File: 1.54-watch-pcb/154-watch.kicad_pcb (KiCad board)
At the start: 4 copper layers, 50 x 32.5 mm, 58 parts, among them J1 AFC24-S24FIC-00, J2 Conn_01x06_Female, J3 USB_C_Programming, J4 Jack-DC, J5 Conn_01x02_Male, Q1 Si1308, Q2 BC817, Q3 BC817, Q4 Si2301CDS, SW1 RESET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

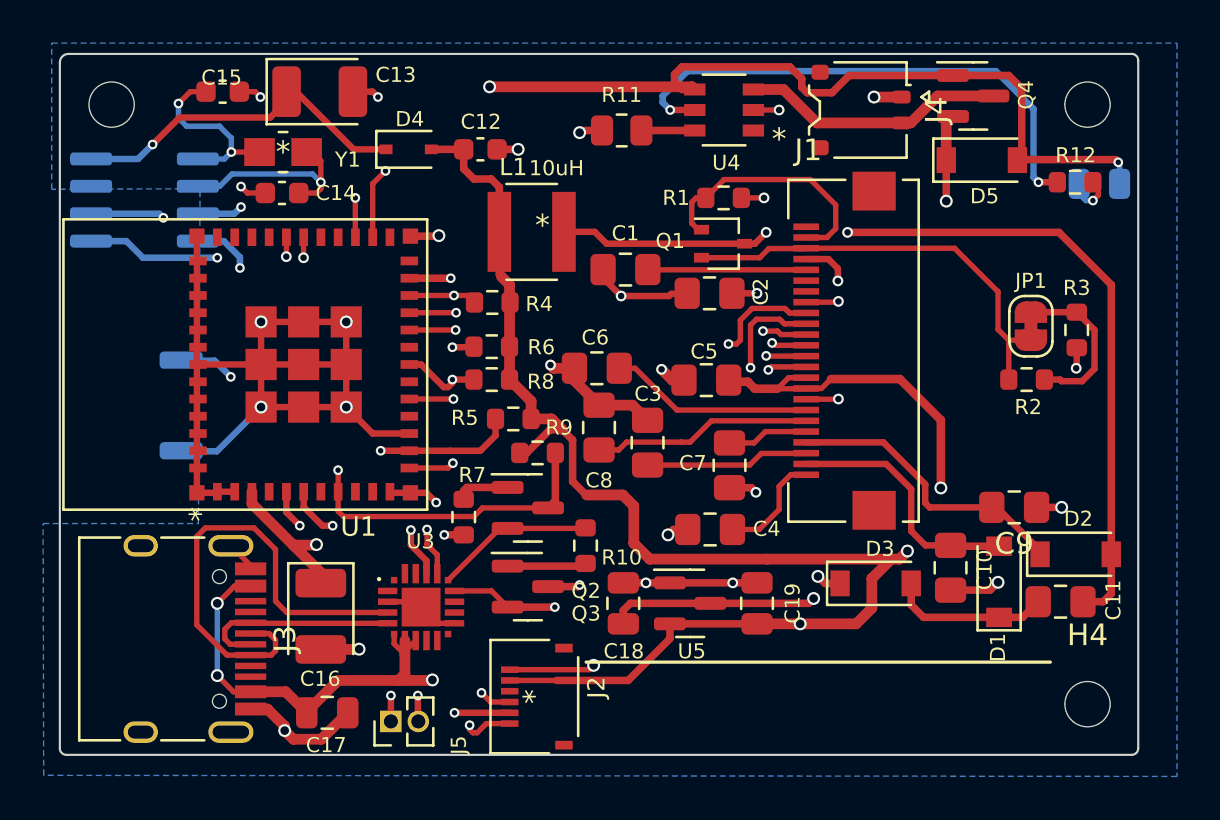
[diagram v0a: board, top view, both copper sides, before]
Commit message: #6 Make edge cut for FPC
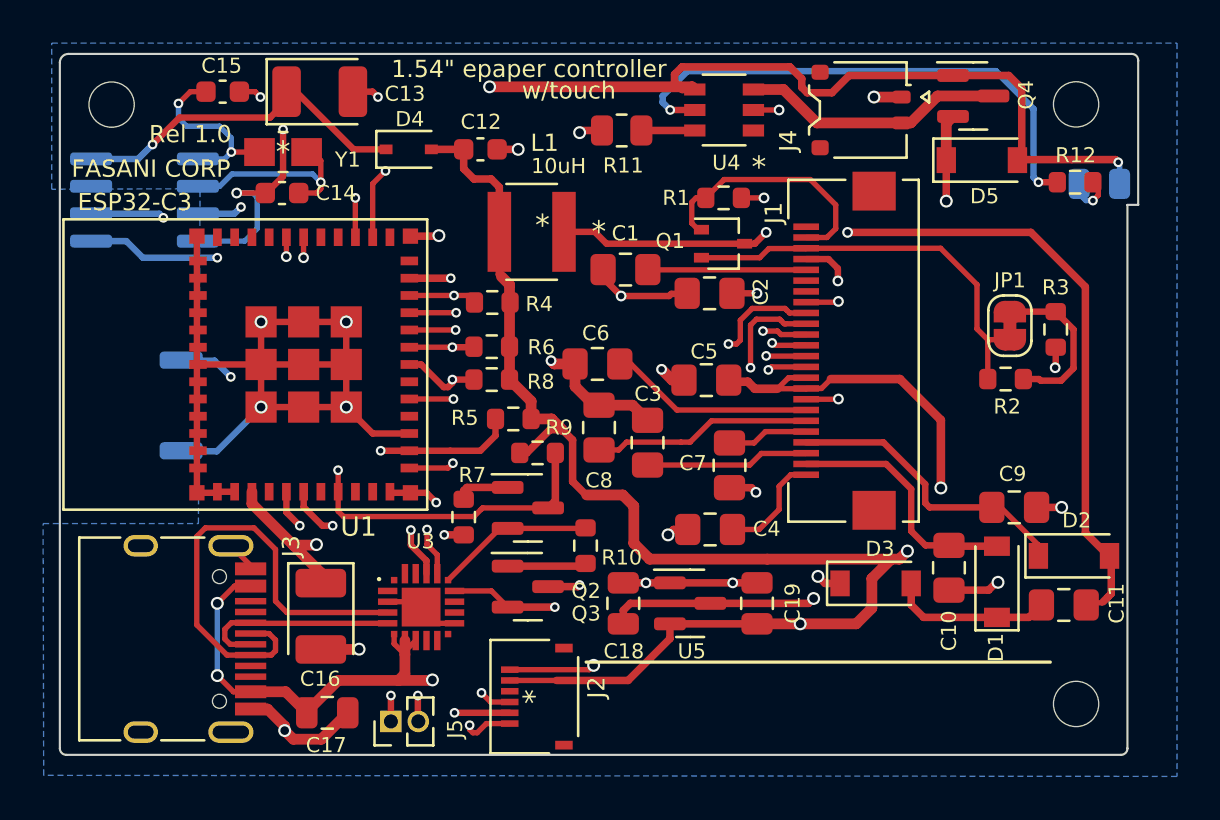
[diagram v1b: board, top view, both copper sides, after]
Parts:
- U1: value ESP32-C3-MINI-1-N4 -> ESP32-C3-MINI
- U4: value TP4057-42-SOT26-R -> SOT-23-5_TPW
- moved JP1 0.98 mm to (116.0, 42.6)
- moved R2 0.98 mm to (115.8, 45.1)
- moved R3 0.98 mm to (118.2, 42.8)
- moved H3 0.53 mm to (119.1, 32.3)
- moved H4 0.53 mm to (119.1, 60.1)
- moved C11 0.21 mm to (118.5, 55.5)
- moved C6 0.20 mm to (96.9, 44.4)
- moved D2 0.11 mm to (119.0, 53.3)
- moved D1 0.10 mm to (115.5, 54.5)
- moved C10 0.08 mm to (113.2, 53.8)
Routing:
- net GND: track 102.0 -> 108.3 mm
- net /I2C_SDA: track 43.0 -> 44.9 mm
- net Net-(J1-Pad22): track 20.1 -> 19.3 mm
- net Net-(C11-Pad2): track 42.6 -> 42.0 mm
- net PREVGH: track 13.6 -> 14.2 mm
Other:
- outline, holes or cut-outs redrawn
- board text added: "1.54{dblquote} epaper controller"
- board text added: "200x200 with optional touch panel"
- board text added: "ESP32-C3"
- board text added: "FASANI CORP"
- board text added: "GOOD-DISPLAY GDEY0154D67"
- board text added: "Rel 1.0"
- board text added: "w/touch"

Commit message: #6 Add info to silk
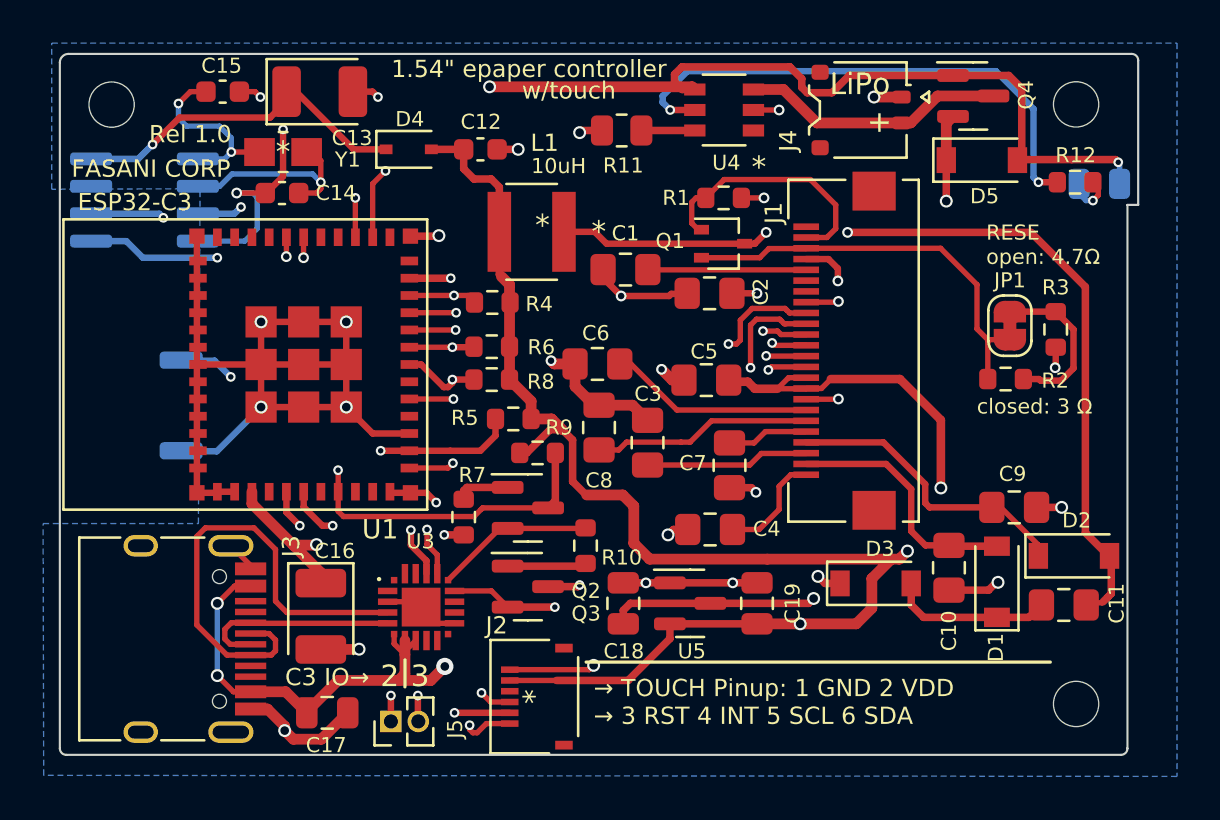
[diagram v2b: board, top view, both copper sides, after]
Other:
- board text added: "+"
- board text added: "2"
- board text added: "200x200 with optional touch panel PCF8563 RTC"
- board text added: "3"
- board text added: "C3 IO→"
- board text added: "GOOD DISPLAY GDEY0154D67"
- board text added: "LiPo"
- board text added: "RESE open: 4.7Ω"
- board text added: "RST→"
- board text added: "closed: 3 Ω"
- board text added: "→ TOUCH Pinup: 1 GND 2 VDD → 3 RST 4 INT 5 SCL 6 SDA"
- board text added: "→CHARGE RDY"
- board text removed: "200x200 with optional touch panel"
- board text removed: "GOOD-DISPLAY GDEY0154D67"
